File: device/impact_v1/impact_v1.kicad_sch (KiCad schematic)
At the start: 5 parts

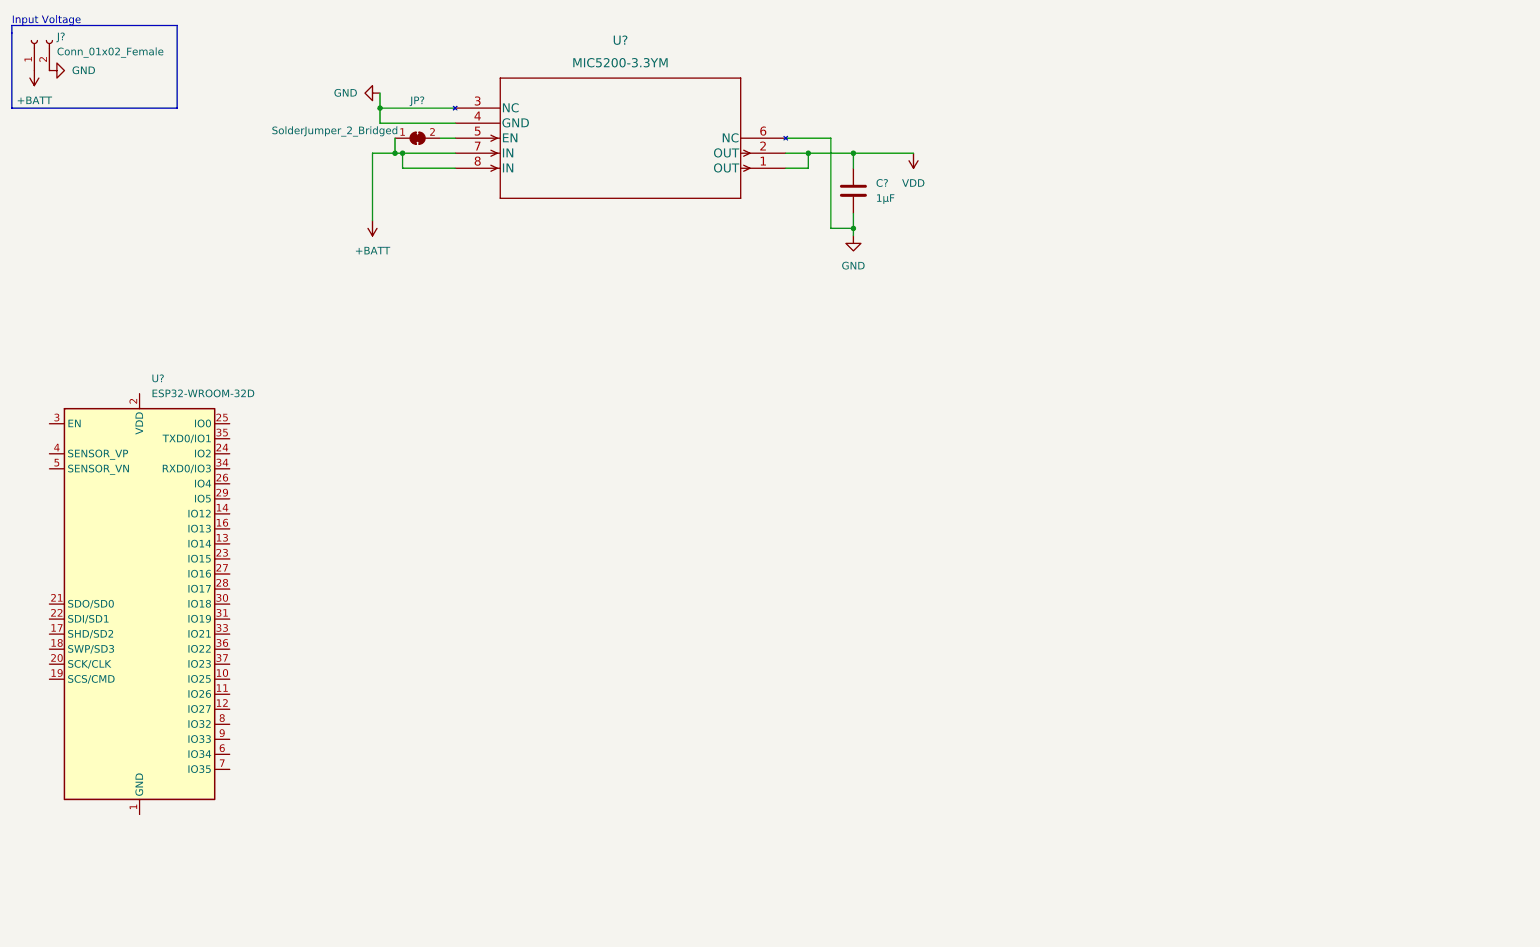
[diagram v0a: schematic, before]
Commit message: Finished ADXL375
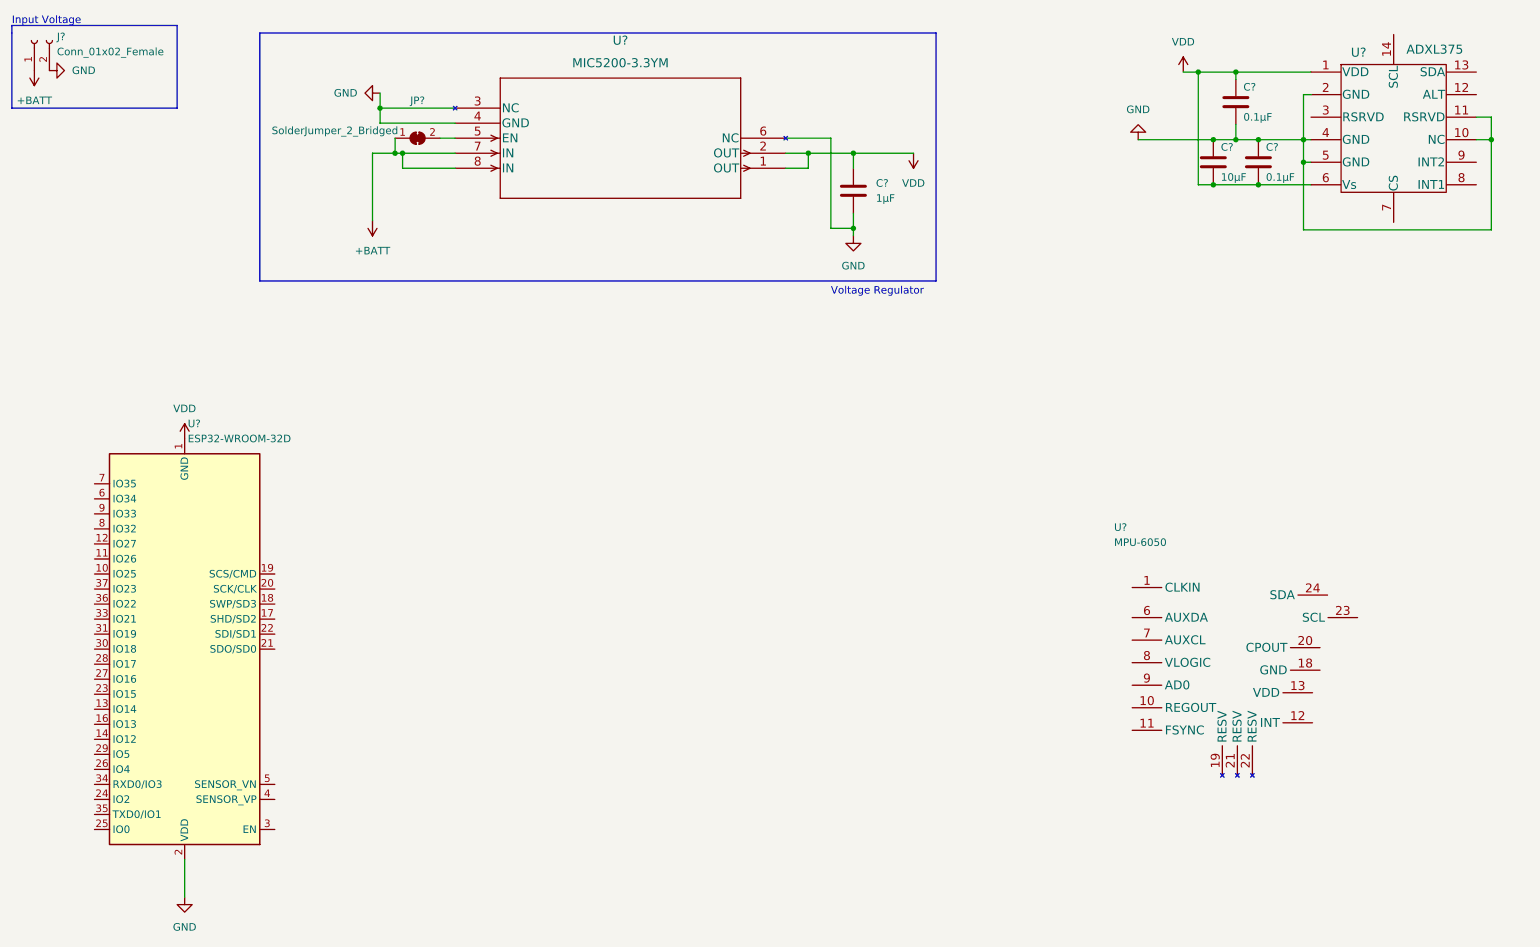
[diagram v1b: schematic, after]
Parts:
- added C? (x2): 0.1µF, symbol Device:C
- added C?: 10µF, symbol Device:C
- added U?: ADXL375, Sensor_Motion:ADXL375BCCZ, symbol Sensor_Motion:ADXL375BCCZ
- added U?: MPU-6050, Sensor_Motion:InvenSense_QFN-24_4x4mm_P0.5mm, symbol Sensor_Motion:MPU-6050
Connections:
- net GND: now also U?.2 (VDD), C?.1, C?.1, C?.2, U?.10 (NC), U?.11 (RSRVD), U?.2 (GND), U?.4 (GND), U?.5 (GND)
- net VDD: now also U?.1 (GND), U?.15 (GND), U?.38 (GND), U?.39 (GND), C?.1, C?.2, C?.2, U?.1 (VDD), U?.6 (Vs)
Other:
- note added: "Voltage Regulator"
- moved on the sheet: U?

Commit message: Finished Schematics
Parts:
- added C1: 0.01µF, symbol Device:C_Small
- added C10: 10µF, symbol Device:C_Small
- added C11, C3, C9: 0.1µF, symbol Device:C_Small
- added C6: 2200pF, symbol Device:C_Small
- added C7: 0.1µF, symbol Device:C
- added R1, R2: 2.2K, Resistor_SMD:R_2512_6332Metric_Pad1.40x3.35mm_HandSolder, symbol Device:R
- added R3: 10k, Resistor_SMD:R_1206_3216Metric_Pad1.30x1.75mm_HandSolder, symbol Device:R
- JP1: renamed from JP?; footprint (none) -> Jumper:SolderJumper-2_P1.3mm_Bridged_RoundedPad1.0x1.5mm
- U1: renamed from U?; footprint Voltage_Regulator_Linear:MIC5200-3.3YM -> Resistor_SMD:R_0603_1608Metric_Pad0.98x0.95mm_HandSolder
- gave numbers to parts that had none: 8
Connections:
- net GND: now also U2.11 (FSYNC), U2.18 (GND), C1.2, C10.2, C11.2, C3.2, C6.2, C7.2, C9.2; no longer U4.2 (VDD)
- net VDD: now also U2.12 (INT), U2.13 (VDD), U4.2 (VDD), U4.29 (IO5), C10.1, C11.1, C7.1, R1.1, R2.1, R3.1; no longer U4.1 (GND), U4.15 (GND), U4.38 (GND), U4.39 (GND)
- net at U3.13 (SDA): now also U2.24 (SDA), U4.21 (SDO/SD0), R2.2
- net at U3.14 (SCL): now also U2.23 (SCL), U4.22 (SDI/SD1), R1.2
- net at U3.8 (INT1): now also U4.31 (IO19)
- net at U3.9 (INT2): now also U4.30 (IO18)
- net at U2.10 (REGOUT): now also C3.1
- net at U2.20 (CPOUT): now also C6.1
- net at U2.8 (VLOGIC): now also C1.1
- net at U4.3 (EN): now also C9.1, R3.2
- new net: U4.1 (GND), U4.15 (GND), U4.38 (GND), U4.39 (GND)
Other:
- moved on the sheet: C2, C4, C5, U3, U4

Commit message: Added Footprints
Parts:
- added D?: D_Schottky, symbol Device:D_Schottky
- C1: footprint (none) -> Capacitor_SMD:C_0603_1608Metric_Pad1.08x0.95mm_HandSolder
- C10, C11, C3, C4, C5, C7, C9: footprint (none) -> Capacitor_SMD:C_0201_0603Metric_Pad0.64x0.40mm_HandSolder
- C6, C8: footprint (none) -> Capacitor_SMD:C_0402_1005Metric_Pad0.74x0.62mm_HandSolder
- R1, R2: footprint Resistor_SMD:R_2512_6332Metric_Pad1.40x3.35mm_HandSolder -> Resistor_SMD:R_0201_0603Metric_Pad0.64x0.40mm_HandSolder
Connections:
- net +BATT: now also D?.2 (A); no longer JP1.1 (A), U1.7 (IN), U1.8 (IN)
- new net: D?.1 (K), JP1.1 (A), U1.7 (IN), U1.8 (IN)
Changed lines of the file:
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@@
+    (stroke (width 0) (type default) (color 0 0 0 0))
+  )
+  (wire (pts (xy 68.707 51.816) (xy 68.707 50.8))
     (stroke (width 0) (type default) (color 0 0 0 0))
   )
@@
     (stroke (width 0) (type default) (color 0 0 0 0))
   )
+  (wire (pts (xy 78.994 50.8) (xy 82.55 50.8))
+    (stroke (width 0) (type default) (color 0 0 0 0))
+  )
   (wire (pts (xy 146.05 115.57) (xy 161.29 115.57))
     (stroke (width 0) (type default) (color 0 0 0 0))
@@
   )
   (wire (pts (xy 127.635 99.06) (xy 130.175 99.06))
+    (stroke (width 0) (type default) (color 0 0 0 0))
+  )
+  (wire (pts (xy 68.707 50.8) (xy 71.374 50.8))
     (stroke (width 0) (type default) (color 0 0 0 0))
   )
@@
   (text "Input Voltage" (at 21.59 17.78 0)
     (effects (font (size 1.27 1.27)) (justify left bottom))
+  )
+  (symbol (lib_id "Device:D_Schottky") (at 75.184 50.8 180) (unit 1)
+    (in_bom yes) (on_board yes) (fields_autoplaced)
+    (property "Reference" "D?" (id 0) (at 75.5015 44.45 0))
+    (property "Value" "D_Schottky" (id 1) (at 75.5015 46.99 0))
+    (property "Footprint" "" (id 2) (at 75.184 50.8 0)
+      (effects (font (size 1.27 1.27)) hide)
+    )
+    (property "Datasheet" "~" (id 3) (at 75.184 50.8 0)
+      (effects (font (size 1.27 1.27)) hide)
+    )
+    (pin "1")
+    (pin "2")
   )
   (symbol (lib_id "Device:C") (at 86.995 92.71 0) (unit 1)
@@
       (effects (font (size 1.27 1.27)) (justify left))
     )
-    (property "Footprint" "" (id 2) (at 87.9602 96.52 0)
+    (property "Footprint" "Capacitor_SMD:C_0201_0603Metric_Pad0.64x0.40mm_HandSolder" (id 2) (at 87.9602 96.52 0)
       (effects (font (size 1.27 1.27)) hide)
     )
@@
       (effects (font (size 1.27 1.27)) (justify left))
     )
-    (property "Footprint" "" (id 2) (at 212.725 90.805 0)
+    (property "Footprint" "Capacitor_SMD:C_0201_0603Metric_Pad0.64x0.40mm_HandSolder" (id 2) (at 212.725 90.805 0)
       (effects (font (size 1.27 1.27)) hide)
     )
@@
       (effects (font (size 1.27 1.27)) (justify left))
     )
-    (property "Footprint" "Resistor_SMD:R_2512_6332Metric_Pad1.40x3.35mm_HandSolder" (id 2) (at 170.942 93.98 90)
+    (property "Footprint" "Resistor_SMD:R_0201_0603Metric_Pad0.64x0.40mm_HandSolder" (id 2) (at 170.942 93.98 90)
       (effects (font (size 1.27 1.27)) hide)
     )
@@
       (effects (font (size 1.27 1.27)) (justify left))
     )
-    (property "Footprint" "" (id 2) (at 259.715 64.77 0)
+    (property "Footprint" "Capacitor_SMD:C_0201_0603Metric_Pad0.64x0.40mm_HandSolder" (id 2) (at 259.715 64.77 0)
       (effects (font (size 1.27 1.27)) hide)
     )
@@
       (effects (font (size 1.27 1.27)) (justify left))
     )
-    (property "Footprint" "" (id 2) (at 131.445 138.43 0)
+    (property "Footprint" "Capacitor_SMD:C_0402_1005Metric_Pad0.74x0.62mm_HandSolder" (id 2) (at 131.445 138.43 0)
       (effects (font (size 1.27 1.27)) hide)
     )
@@
       (effects (font (size 1.27 1.27)) (justify left))
     )
-    (property "Footprint" "" (id 2) (at 91.7702 106.68 0)
+    (property "Footprint" "Capacitor_SMD:C_0201_0603Metric_Pad0.64x0.40mm_HandSolder" (id 2) (at 91.7702 106.68 0)
       (effects (font (size 1.27 1.27)) hide)
     )
@@
       (effects (font (size 1.27 1.27)) (justify left))
     )
-    (property "Footprint" "" (id 2) (at 140.0302 154.94 0)
+    (property "Footprint" "Capacitor_SMD:C_0201_0603Metric_Pad0.64x0.40mm_HandSolder" (id 2) (at 140.0302 154.94 0)
       (effects (font (size 1.27 1.27)) hide)
     )
@@
       (effects (font (size 1.27 1.27)) (justify left))
     )
-    (property "Footprint" "" (id 2) (at 269.875 64.77 0)
+    (property "Footprint" "Capacitor_SMD:C_0201_0603Metric_Pad0.64x0.40mm_HandSolder" (id 2) (at 269.875 64.77 0)
       (effects (font (size 1.27 1.27)) hide)
     )
@@
       (effects (font (size 1.27 1.27)) (justify left))
     )
-    (property "Footprint" "" (id 2) (at 164.7952 49.53 0)
+    (property "Footprint" "Capacitor_SMD:C_0402_1005Metric_Pad0.74x0.62mm_HandSolder" (id 2) (at 164.7952 49.53 0)
       (effects (font (size 1.27 1.27)) hide)
     )
@@
       (effects (font (size 1.27 1.27)) (justify left))
     )
-    (property "Footprint" "Resistor_SMD:R_2512_6332Metric_Pad1.40x3.35mm_HandSolder" (id 2) (at 181.102 93.98 90)
+    (property "Footprint" "Resistor_SMD:R_0201_0603Metric_Pad0.64x0.40mm_HandSolder" (id 2) (at 181.102 93.98 90)
       (effects (font (size 1.27 1.27)) hide)
     )
@@
       (effects (font (size 1.27 1.27)) (justify left))
     )
-    (property "Footprint" "" (id 2) (at 78.105 147.32 0)
+    (property "Footprint" "Capacitor_SMD:C_0603_1608Metric_Pad1.08x0.95mm_HandSolder" (id 2) (at 78.105 147.32 0)
       (effects (font (size 1.27 1.27)) hide)
     )
@@
       (effects (font (size 1.27 1.27)) (justify left))
     )
-    (property "Footprint" "" (id 2) (at 85.725 147.32 0)
+    (property "Footprint" "Capacitor_SMD:C_0201_0603Metric_Pad0.64x0.40mm_HandSolder" (id 2) (at 85.725 147.32 0)
       (effects (font (size 1.27 1.27)) hide)
     )
@@
     (pin "2")
   )
-  (symbol (lib_id "power:+BATT") (at 82.55 50.8 180) (unit 1)
-    (in_bom yes) (on_board yes) (fields_autoplaced)
-    (property "Reference" "#PWR0105" (id 0) (at 82.55 46.99 0)
-      (effects (font (size 1.27 1.27)) hide)
-    )
-    (property "Value" "+BATT" (id 1) (at 82.55 55.88 0))
-    (property "Footprint" "" (id 2) (at 82.55 50.8 0)
-      (effects (font (size 1.27 1.27)) hide)
-    )
-    (property "Datasheet" "" (id 3) (at 82.55 50.8 0)
+  (symbol (lib_id "power:+BATT") (at 68.707 51.816 180) (unit 1)
+    (in_bom yes) (on_board yes) (fields_autoplaced)
+    (property "Reference" "#PWR0105" (id 0) (at 68.707 48.006 0)
+      (effects (font (size 1.27 1.27)) hide)
+    )
+    (property "Value" "+BATT" (id 1) (at 68.707 57.277 0))
+    (property "Footprint" "" (id 2) (at 68.707 51.816 0)
+      (effects (font (size 1.27 1.27)) hide)
+    )
+    (property "Datasheet" "" (id 3) (at 68.707 51.816 0)
       (effects (font (size 1.27 1.27)) hide)
     )
@@
     )
     (path "/c8b37e48-efbc-407b-86cc-d21552e503c0"
-      (reference "C1") (unit 1) (value "0.01µF") (footprint "")
+      (reference "C1") (unit 1) (value "0.01µF") (footprint "Capacitor_SMD:C_0603_1608Metric_Pad1.08x0.95mm_HandSolder")
     )
     (path "/7d055ff3-b74e-4956-8b71-3a0ca903a084"
@@
     )
     (path "/e660224e-d104-4e5c-999b-5cae380c0786"
-      (reference "C3") (unit 1) (value "0.1µF") (footprint "")
+      (reference "C3") (unit 1) (value "0.1µF") (footprint "Capacitor_SMD:C_0201_0603Metric_Pad0.64x0.40mm_HandSolder")
     )
     (path "/1619fbb1-b719-448d-aa0d-10c3e8143e7a"
-      (reference "C4") (unit 1) (value "0.1µF") (footprint "")
+      (reference "C4") (unit 1) (value "0.1µF") (footprint "Capacitor_SMD:C_0201_0603Metric_Pad0.64x0.40mm_HandSolder")
     )
     (path "/92680097-aa2a-4b3f-b8b7-acae287f0c04"
-      (reference "C5") (unit 1) (value "0.1µF") (footprint "")
+      (reference "C5") (unit 1) (value "0.1µF") (footprint "Capacitor_SMD:C_0201_0603Metric_Pad0.64x0.40mm_HandSolder")
     )
     (path "/91b1515f-01d7-467f-9976-fa4a3565e617"
-      (reference "C6") (unit 1) (value "2200pF") (footprint "")
+      (reference "C6") (unit 1) (value "2200pF") (footprint "Capacitor_SMD:C_0402_1005Metric_Pad0.74x0.62mm_HandSolder")
     )
     (path "/9b5a65ed-ee9b-47bc-95cf-22d10607dabe"
-      (reference "C7") (unit 1) (value "0.1µF") (footprint "")
+      (reference "C7") (unit 1) (value "0.1µF") (footprint "Capacitor_SMD:C_0201_0603Metric_Pad0.64x0.40mm_HandSolder")
     )
     (path "/b3b7e848-5cf5-4f15-bcf7-1e0a5d787cbb"
-      (reference "C8") (unit 1) (value "1µF") (footprint "")
+      (reference "C8") (unit 1) (value "1µF") (footprint "Capacitor_SMD:C_0402_1005Metric_Pad0.74x0.62mm_HandSolder")
     )
     (path "/34ccbb51-20ab-4e56-9cdf-008a1f94c805"
-      (reference "C9") (unit 1) (value "0.1µF") (footprint "")
+      (reference "C9") (unit 1) (value "0.1µF") (footprint "Capacitor_SMD:C_0201_0603Metric_Pad0.64x0.40mm_HandSolder")
     )
     (path "/91390cfe-15b2-4402-8118-94f5da7ab8d6"
-      (reference "C10") (unit 1) (value "10µF") (footprint "")
+      (reference "C10") (unit 1) (value "10µF") (footprint "Capacitor_SMD:C_0201_0603Metric_Pad0.64x0.40mm_HandSolder")
     )
     (path "/9e94dbbe-53bf-4cd4-bd0c-9456d119dddd"
-      (reference "C11") (unit 1) (value "0.1µF") (footprint "")
+      (reference "C11") (unit 1) (value "0.1µF") (footprint "Capacitor_SMD:C_0201_0603Metric_Pad0.64x0.40mm_HandSolder")
+    )
+    (path "/035ad69b-101d-4a07-9109-768fd21ef62f"
+      (reference "D?") (unit 1) (value "D_Schottky") (footprint "")
     )
     (path "/eb1c0288-1a6c-49e8-b97d-d84c22124b1e"
@@
     )
     (path "/403cdc06-5d0d-44f7-b7e8-fc665133a24c"
-      (reference "R1") (unit 1) (value "2.2K") (footprint "Resistor_SMD:R_2512_6332Metric_Pad1.40x3.35mm_HandSolder")
+      (reference "R1") (unit 1) (value "2.2K") (footprint "Resistor_SMD:R_0201_0603Metric_Pad0.64x0.40mm_HandSolder")
     )
     (path "/b7e58d78-4b5f-456a-b7c4-bdc7ed4f9d18"
-      (reference "R2") (unit 1) (value "2.2K") (footprint "Resistor_SMD:R_2512_6332Metric_Pad1.40x3.35mm_HandSolder")
+      (reference "R2") (unit 1) (value "2.2K") (footprint "Resistor_SMD:R_0201_0603Metric_Pad0.64x0.40mm_HandSolder")
     )
     (path "/2846bab3-5cbb-47dd-ba45-bbd907438830"
